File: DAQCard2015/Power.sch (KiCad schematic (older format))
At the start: 33 parts, among them CON1 BARREL_JACK, SW1 SPST, U19 CDBHD240-G, U20 LM1086, U21 APXS002A0X-SRZ, U22 APXS002A0X-SRZ, U23 APXS002A0X-SRZ

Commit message: Various updates to DAQ board focusing on power system
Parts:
- removed C56, C57, C58: 100uF, extras:SMD_Cap_8mmDia, symbol CP
- removed C60, C61: 10uF, Capacitors_SMD:C_0805, symbol C
- removed C62, C63: 10000pF, Capacitors_SMD:C_0603, symbol C
- removed C64: 3900pF, Capacitors_SMD:C_0603, symbol C
- removed C65, C66, C67, C68, C69: 47uF, extras:SMD_Cap_8mmDia, symbol C
- removed D1: LED, LEDs:LED-1206, symbol LED
- removed R50: 220R, Resistors_SMD:R_0603, symbol R
- removed R51: 2.22k, Resistors_SMD:R_0603, symbol R
- removed R52: 150R, Resistors_SMD:R_0603, symbol R
- removed SW1: SPST, extras:Switch_ES02MSABE, symbol SPST
- removed U19: CDBHD240-G, extras:mini-DIP4, symbol CDBHD240-G
- removed U21, U22, U23: APXS002A0X-SRZ, extras:APXS002A0X-SRZ, symbol APXS002A0X-SRZ
- added C56: 0.47uF, Capacitors_SMD:C_0603, symbol C
- added C57: 47uF, extras:SMD_Cap_8mmDia, symbol C
- added C58: 10uF, Capacitors_SMD:C_0805, symbol C
- added D4: MBRA340, Diodes_SMD:SMA_Standard, symbol D_Schottky_Small
- added DB1: NMLU1210, extras:NMLU1210, symbol NMLU1210
- added L1: 5.6uH, extras:SLF101, symbol INDUCTOR_SMALL
- added SW1: DPDT, extras:DFXX-XX-X-XX-A-X-XX, symbol DPDT
- added U21: LT1913, extras:LT1913, symbol LT1913
- C53: value 100uF -> 22uF
- C55: value 10uF -> 680pF; footprint Capacitors_SMD:C_0805 -> Capacitors_SMD:C_0603
- C59: value 10uF -> .1uF; footprint Capacitors_SMD:C_0805 -> Capacitors_SMD:C_0603
- R46: value 150R -> 63.4k
- R47: value 5k -> 15k
- R48: value 150R -> 100k
- R49: value 5k -> 536k
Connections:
- net labels removed: 1V8dig, GNDdig
- wire segments 94 -> 51
- no-connect marks 6 -> 3
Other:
- note added: "Al"
- note added: "Cer"
- note added: "Required Power Nets:\n5Vdig\n -->500mA(1V8ana)\n -->110mA(1V8dig)\n -->180mA(fan)\n -->600mA(ZEM)\n-5Vdig(Not Used)\n3.3Vdig\n1V8dig(32mA*8=256mA)\n1V8ana(142mA*8=1.136A)"
- note added: "Wall Jack\n |--->5V Switching Reg\n |--->1.8Vana Linear Reg\n |--->ZEM(3.3V) Switching Reg\n |--->ZEM(1.8V(dig)) Linear Reg\n"
- note removed: "Power Indicator LED"
- note removed: "Required Power Nets:\n5Vdig\n -->500mA(1V8ana)\n -->110mA(1V8dig)\n -->180mA(fan)\n-5Vdig(Not Used)\n3.3Vdig\n1V8dig(32mA*8=256mA)\n1V8ana(142mA*8=1.136A)"
- moved on the sheet: C53, C54, U20

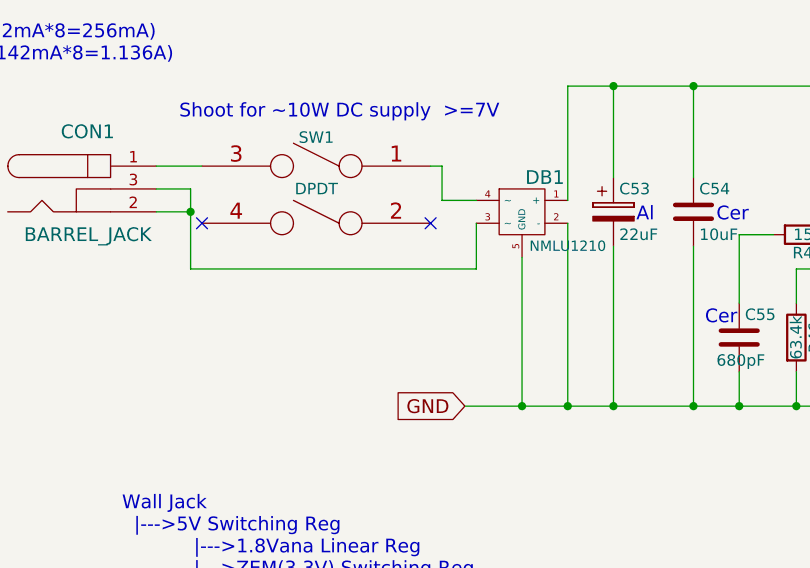
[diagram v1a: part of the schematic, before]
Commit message: Updates to DAQ Board focusing on the power system and flood fills for it
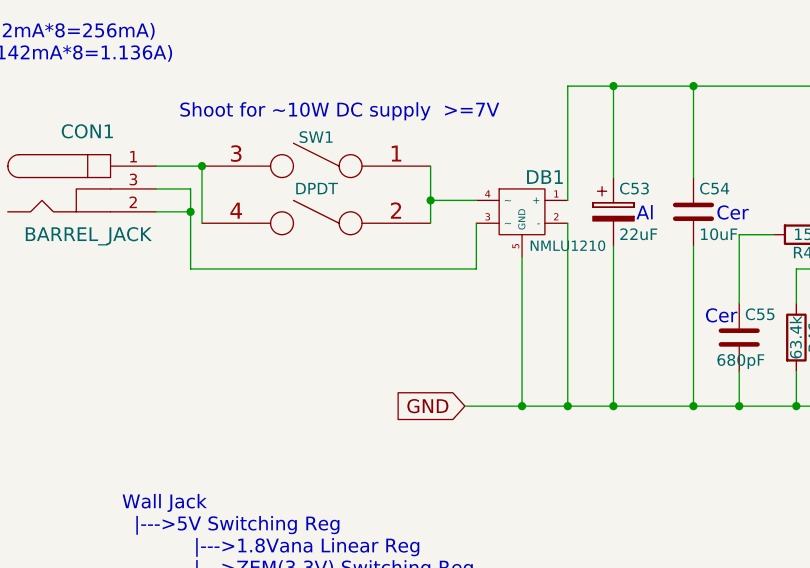
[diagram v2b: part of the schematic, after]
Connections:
- net at CON1.1, SW1.3: now also SW1.4
- net at DB1.4 (~~), SW1.1: now also SW1.2
- no-connect marks 3 -> 1
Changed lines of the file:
@@
 $Descr A4 11693 8268
 encoding utf-8
-Sheet 13 13
+Sheet 4 13
 Title ""
 Date ""
@@
 	-1   0    0    -1
 $EndComp
-NoConn ~ 2950 2100
-NoConn ~ 1950 2100
 $Comp
 L C C58
@@
 Text Notes 1600 3750 0    60   ~ 0
 Wall Jack\n  |--->5V Switching Reg\n            |--->1.8Vana Linear Reg\n            |--->ZEM(3.3V) Switching Reg\n            |--->ZEM(1.8V(dig)) Linear Reg\n
-Wire Wire Line
-	1900 2050 1750 2050
-Wire Wire Line
-	1750 1950 1900 1950
-Wire Wire Line
-	1900 1950 1900 2300
-Connection ~ 1900 2050
-Wire Wire Line
-	1750 1850 1950 1850
-Wire Wire Line
-	2950 1850 3000 1850
-Wire Wire Line
-	3550 1500 5200 1500
-Wire Wire Line
-	3750 1500 3750 1900
-Wire Wire Line
-	3750 2200 3750 2900
-Connection ~ 3750 2900
-Wire Wire Line
-	4100 2900 4100 2200
-Connection ~ 4100 2900
-Wire Wire Line
-	4100 1500 4100 1900
-Connection ~ 3750 1500
-Connection ~ 4100 1500
-Wire Wire Line
-	3000 1850 3000 2000
-Wire Wire Line
-	3000 2000 3150 2000
-Wire Wire Line
-	3550 2100 3550 2900
-Wire Wire Line
-	3100 2900 8950 2900
-Wire Wire Line
-	3550 2000 3550 1500
-Wire Wire Line
-	1900 2300 3150 2300
-Wire Wire Line
-	3150 2300 3150 2100
-Wire Wire Line
-	6550 2150 7800 2150
-Wire Wire Line
-	8300 2100 8350 2100
-Wire Wire Line
-	8350 2100 8350 2150
-Wire Wire Line
-	8300 2150 9050 2150
-Connection ~ 8350 2150
-Wire Wire Line
-	8050 2900 8050 2350
-Connection ~ 8700 2150
-Wire Wire Line
-	8700 2900 8700 2650
-Connection ~ 8050 2900
-Wire Wire Line
-	8950 2900 8950 2650
-Connection ~ 8700 2900
-Connection ~ 8950 2150
-Wire Wire Line
-	5350 2900 5350 2700
-Wire Wire Line
-	5200 1500 5200 1600
-Wire Wire Line
-	4950 2150 4750 2150
-Wire Wire Line
-	4450 2150 4300 2150
-Wire Wire Line
-	4300 2150 4300 2450
-Wire Wire Line
-	4300 2750 4300 2900
-Connection ~ 4300 2900
-Wire Wire Line
-	4950 2300 4550 2300
-Wire Wire Line
-	4550 2300 4550 2450
-Wire Wire Line
-	4550 2750 4550 2900
-Connection ~ 4550 2900
-Wire Wire Line
-	4950 2500 4800 2500
-Wire Wire Line
-	4800 2500 4800 2900
-Connection ~ 4800 2900
-Wire Wire Line
-	5500 1600 5500 1500
-Wire Wire Line
-	5750 2150 6050 2150
-Wire Wire Line
-	6000 2050 6000 2250
-Connection ~ 6000 2150
-Wire Wire Line
-	5750 2000 5750 1750
-Wire Wire Line
-	5750 1750 6000 1750
-Wire Wire Line
-	5850 2900 5850 2850
-Connection ~ 5350 2900
-Connection ~ 5850 2900
-Wire Wire Line
-	5750 2550 6100 2550
-Wire Wire Line
-	5750 2550 5750 2500
-Connection ~ 5850 2550
-Wire Wire Line
-	6600 1500 6600 2600
-Wire Wire Line
-	6600 2550 6400 2550
-Wire Wire Line
-	6000 2450 6000 2900
-Connection ~ 6000 2900
-Wire Wire Line
-	5500 1500 9050 1500
-Connection ~ 6600 2550
-Connection ~ 6600 2150
-Connection ~ 6600 1500
-Connection ~ 6600 2900
-Wire Wire Line
-	8950 2150 8950 2350
-Wire Wire Line
-	8700 2350 8700 2150
 $Comp
 L NMLU1210 DB1
@@
 	-1   0    0    -1
 $EndComp
-Connection ~ 3550 2900
-Wire Wire Line
-	3350 2250 3350 2900
-Connection ~ 3350 2900
 Text Notes 3850 2100 0    60   ~ 0
 Al
@@
 Text Notes 6450 2700 0    60   ~ 0
 Cer
+Connection ~ 2950 2000
+Wire Wire Line
+	1950 1850 1950 2100
+Connection ~ 4950 1500
 Wire Wire Line
 	4950 1900 4950 1500
-Connection ~ 4950 1500
+Connection ~ 3350 2900
+Wire Wire Line
+	3350 2250 3350 2900
+Connection ~ 3550 2900
+Wire Wire Line
+	8700 2350 8700 2150
+Wire Wire Line
+	8950 2150 8950 2350
+Connection ~ 6600 2900
+Connection ~ 6600 1500
+Connection ~ 6600 2150
+Connection ~ 6600 2550
+Wire Wire Line
+	5500 1500 9050 1500
+Connection ~ 6000 2900
+Wire Wire Line
+	6000 2450 6000 2900
+Wire Wire Line
+	6600 2550 6400 2550
+Wire Wire Line
+	6600 1500 6600 2600
+Connection ~ 5850 2550
+Wire Wire Line
+	5750 2550 5750 2500
+Wire Wire Line
+	5750 2550 6100 2550
+Connection ~ 5850 2900
+Connection ~ 5350 2900
+Wire Wire Line
+	5850 2900 5850 2850
+Wire Wire Line
+	5750 1750 6000 1750
+Wire Wire Line
+	5750 2000 5750 1750
+Connection ~ 6000 2150
+Wire Wire Line
+	6000 2050 6000 2250
+Wire Wire Line
+	5750 2150 6050 2150
+Wire Wire Line
+	5500 1600 5500 1500
+Connection ~ 4800 2900
+Wire Wire Line
+	4800 2500 4800 2900
+Wire Wire Line
+	4950 2500 4800 2500
+Connection ~ 4550 2900
+Wire Wire Line
+	4550 2750 4550 2900
+Wire Wire Line
+	4550 2300 4550 2450
+Wire Wire Line
+	4950 2300 4550 2300
+Connection ~ 4300 2900
+Wire Wire Line
+	4300 2750 4300 2900
+Wire Wire Line
+	4300 2150 4300 2450
+Wire Wire Line
+	4450 2150 4300 2150
+Wire Wire Line
+	4950 2150 4750 2150
+Wire Wire Line
+	5200 1500 5200 1600
+Wire Wire Line
+	5350 2900 5350 2700
+Connection ~ 8950 2150
+Connection ~ 8700 2900
+Wire Wire Line
+	8950 2900 8950 2650
+Connection ~ 8050 2900
+Wire Wire Line
+	8700 2900 8700 2650
+Connection ~ 8700 2150
+Wire Wire Line
+	8050 2900 8050 2350
+Connection ~ 8350 2150
+Wire Wire Line
+	8300 2150 9050 2150
+Wire Wire Line
+	8350 2100 8350 2150
+Wire Wire Line
+	8300 2100 8350 2100
+Wire Wire Line
+	6550 2150 7800 2150
+Wire Wire Line
+	3150 2300 3150 2100
+Wire Wire Line
+	1900 2300 3150 2300
+Wire Wire Line
+	3550 2000 3550 1500
+Wire Wire Line
+	3100 2900 8950 2900
+Wire Wire Line
+	3550 2900 3550 2100
+Wire Wire Line
+	2950 2000 3150 2000
+Wire Wire Line
+	2950 1850 2950 2100
+Connection ~ 4100 1500
+Connection ~ 3750 1500
+Wire Wire Line
+	4100 1500 4100 1900
+Connection ~ 4100 2900
+Wire Wire Line
+	4100 2900 4100 2200
+Connection ~ 3750 2900
+Wire Wire Line
+	3750 2900 3750 2200
+Wire Wire Line
+	3750 1500 3750 1900
+Wire Wire Line
+	3550 1500 5200 1500
+Wire Wire Line
+	1750 1850 1950 1850
+Connection ~ 1900 2050
+Wire Wire Line
+	1900 1950 1900 2300
+Wire Wire Line
+	1750 1950 1900 1950
+Wire Wire Line
+	1900 2050 1750 2050
+Connection ~ 1950 1850
 $EndSCHEMATC

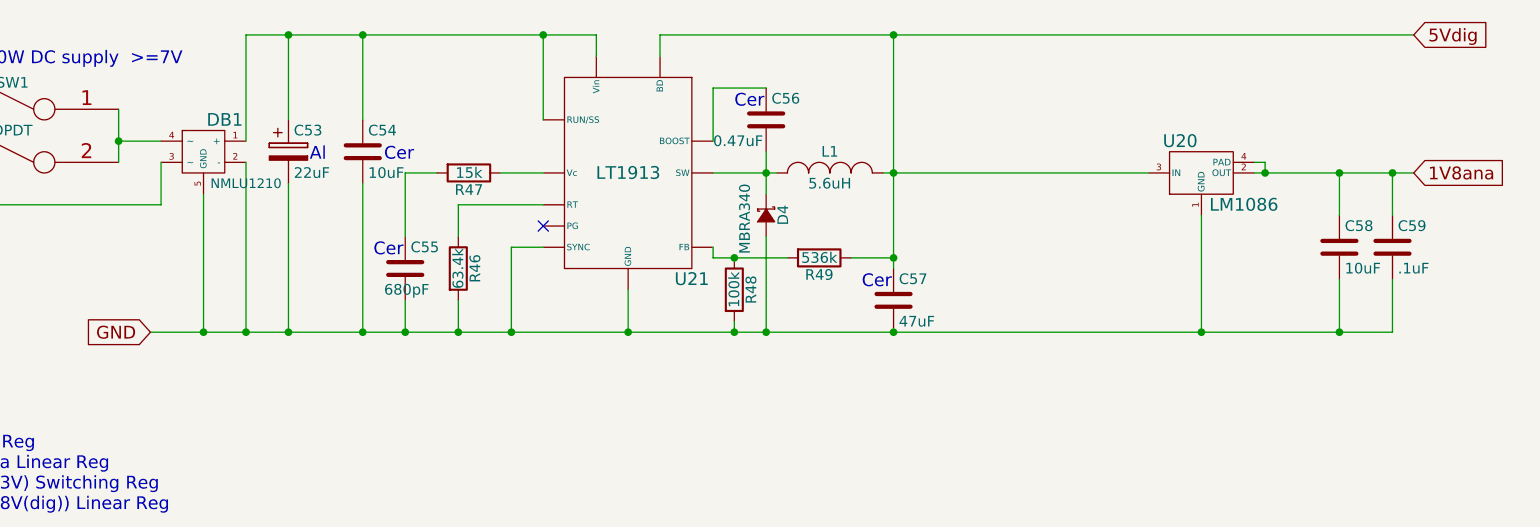
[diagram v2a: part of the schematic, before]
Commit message: Updates to DAQ board focusing on Support electronics
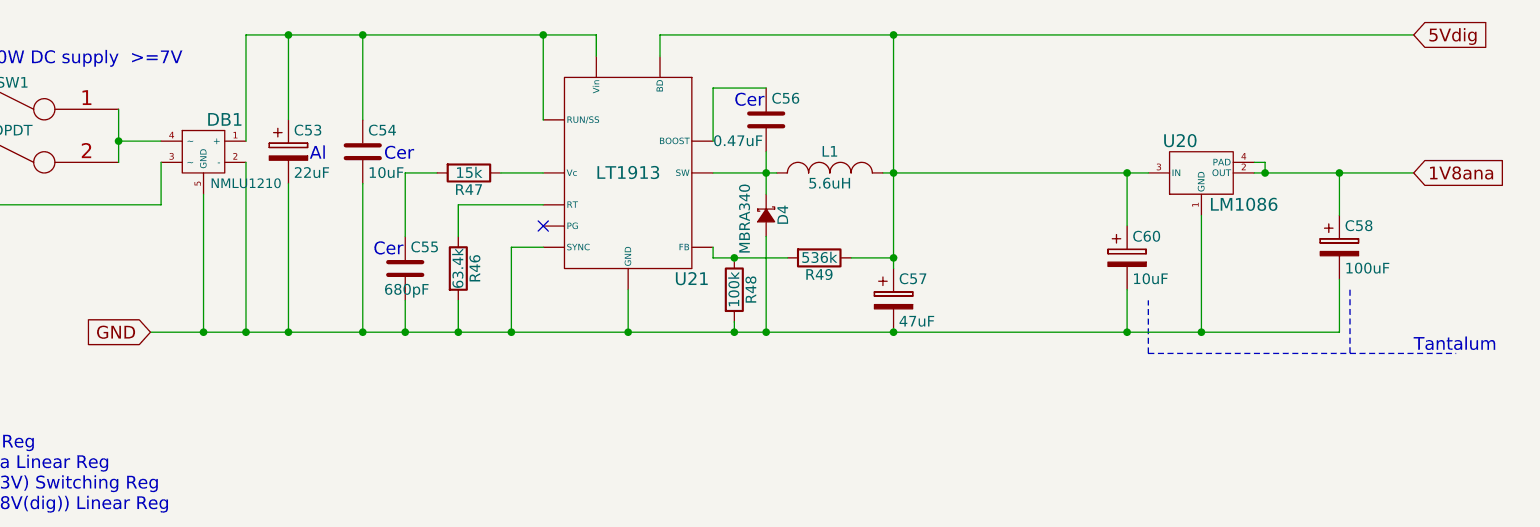
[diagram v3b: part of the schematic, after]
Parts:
- removed C57: 47uF, extras:SMD_Cap_8mmDia, symbol C
- removed C58: 10uF, Capacitors_SMD:C_0805, symbol C
- removed C59: .1uF, Capacitors_SMD:C_0603, symbol C
- added C57: 47uF, Capacitors_Tantalum_SMD:TantalC_SizeD_EIA-7343_Reflow, symbol CP
- added C58: 100uF, Capacitors_Tantalum_SMD:TantalC_SizeD_EIA-7343_Reflow, symbol CP
- added C60: 10uF, Capacitors_Tantalum_SMD:TantalC_SizeD_EIA-7343_Reflow, symbol CP
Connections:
- net 1V8ana: now also C58.1
- net 5Vdig: now also C57.1, C60.1
- net GND: now also C57.2, C58.2, C60.2
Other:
- note added: "Tantalum"
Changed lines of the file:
@@
-$EndComp
-$Comp
-L C C58
-U 1 1 55F899AD
-P 8700 2500
-F 0 "C58" H 8725 2600 50  0000 L CNN
-F 1 "10uF" H 8725 2400 50  0000 L CNN
-F 2 "Capacitors_SMD:C_0805" H 8738 2350 30  0001 C CNN
-F 3 "" H 8700 2500 60  0000 C CNN
-	1    8700 2500
-	1    0    0    -1
-$EndComp
-$Comp
-L C C59
-U 1 1 55F89BBD
-P 8950 2500
-F 0 "C59" H 8975 2600 50  0000 L CNN
-F 1 ".1uF" H 8975 2400 50  0000 L CNN
-F 2 "Capacitors_SMD:C_0603" H 8988 2350 30  0001 C CNN
-F 3 "" H 8950 2500 60  0000 C CNN
-	1    8950 2500
-	1    0    0    -1
 $EndComp
 $Comp
@@
 F 3 "" H 6000 1900 60  0000 C CNN
 	1    6000 1900
-	1    0    0    -1
-$EndComp
-$Comp
-L C C57
-U 1 1 55F8A954
-P 6600 2750
-F 0 "C57" H 6625 2850 50  0000 L CNN
-F 1 "47uF" H 6625 2650 50  0000 L CNN
-F 2 "extras:SMD_Cap_8mmDia" H 6638 2600 30  0001 C CNN
-F 3 "" H 6600 2750 60  0000 C CNN
-	1    6600 2750
 	1    0    0    -1
 $EndComp
@@
 Text Notes 5850 1850 0    60   ~ 0
 Cer
-Text Notes 6450 2700 0    60   ~ 0
-Cer
 Connection ~ 2950 2000
 Wire Wire Line
@@
 Wire Wire Line
 	8700 2350 8700 2150
-Wire Wire Line
-	8950 2150 8950 2350
 Connection ~ 6600 2900
 Connection ~ 6600 1500
@@
 Wire Wire Line
 	5350 2900 5350 2700
-Connection ~ 8950 2150
-Connection ~ 8700 2900
-Wire Wire Line
-	8950 2900 8950 2650
 Connection ~ 8050 2900
 Wire Wire Line
@@
 Wire Wire Line
 	3550 2000 3550 1500
-Wire Wire Line
-	3100 2900 8950 2900
 Wire Wire Line
 	3550 2900 3550 2100
@@
 	1900 2050 1750 2050
 Connection ~ 1950 1850
+Wire Notes Line
+	8750 2700 8750 3000
+Wire Notes Line
+	7800 3000 9250 3000
+Text Notes 9050 3000 0    60   ~ 0
+Tantalum
+$Comp
+L CP C58
+U 1 1 5601F0EE
+P 8700 2500
+F 0 "C58" H 8725 2600 50  0000 L CNN
+F 1 "100uF" H 8725 2400 50  0000 L CNN
+F 2 "Capacitors_Tantalum_SMD:TantalC_SizeD_EIA-7343_Reflow" H 8738 2350 30  0001 C CNN
+F 3 "" H 8700 2500 60  0000 C CNN
+	1    8700 2500
+	1    0    0    -1
+$EndComp
+$Comp
+L CP C60
+U 1 1 5601FD97
+P 7700 2550
+F 0 "C60" H 7725 2650 50  0000 L CNN
+F 1 "10uF" H 7725 2450 50  0000 L CNN
+F 2 "Capacitors_Tantalum_SMD:TantalC_SizeD_EIA-7343_Reflow" H 7738 2400 30  0001 C CNN
+F 3 "" H 7700 2550 60  0000 C CNN
+	1    7700 2550
+	1    0    0    -1
+$EndComp
+Wire Wire Line
+	7700 2700 7700 2900
+Connection ~ 7700 2900
+Wire Wire Line
+	7700 2400 7700 2150
+Connection ~ 7700 2150
+Wire Notes Line
+	7800 3000 7800 2750
+Wire Wire Line
+	3100 2900 8700 2900
+$Comp
+L CP C57
+U 1 1 56021674
+P 6600 2750
+F 0 "C57" H 6625 2850 50  0000 L CNN
+F 1 "47uF" H 6625 2650 50  0000 L CNN
+F 2 "Capacitors_Tantalum_SMD:TantalC_SizeD_EIA-7343_Reflow" H 6638 2600 30  0001 C CNN
+F 3 "" H 6600 2750 60  0000 C CNN
+	1    6600 2750
+	1    0    0    -1
+$EndComp
 $EndSCHEMATC
